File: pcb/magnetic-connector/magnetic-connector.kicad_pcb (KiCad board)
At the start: 2 copper layers, 26 x 24 mm, 14 parts, among them J10 MAG_CONN_IN, J7 VIK_IN, J8 VIK_OUT, J9 MAG_CONN_OUT

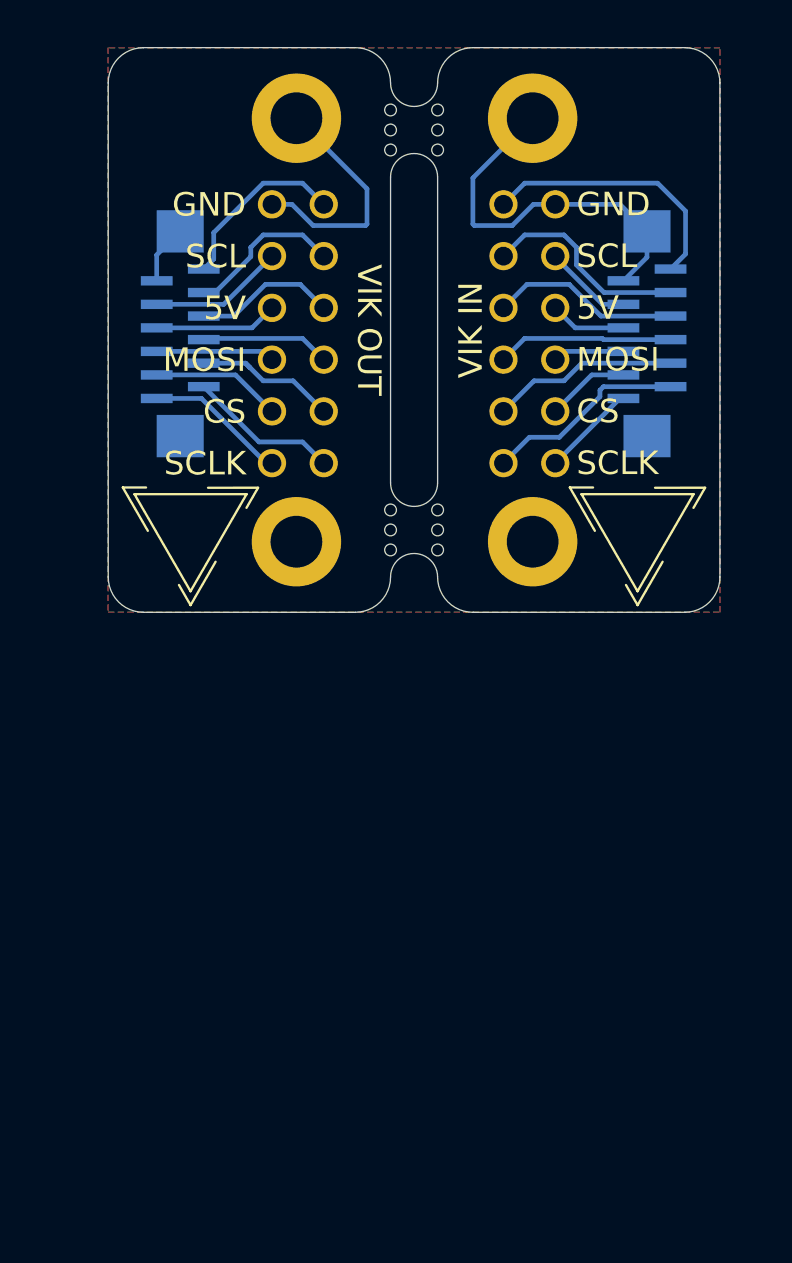
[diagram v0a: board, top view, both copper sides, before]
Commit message: Make magnetic connector size compliant with VIK small form factor.
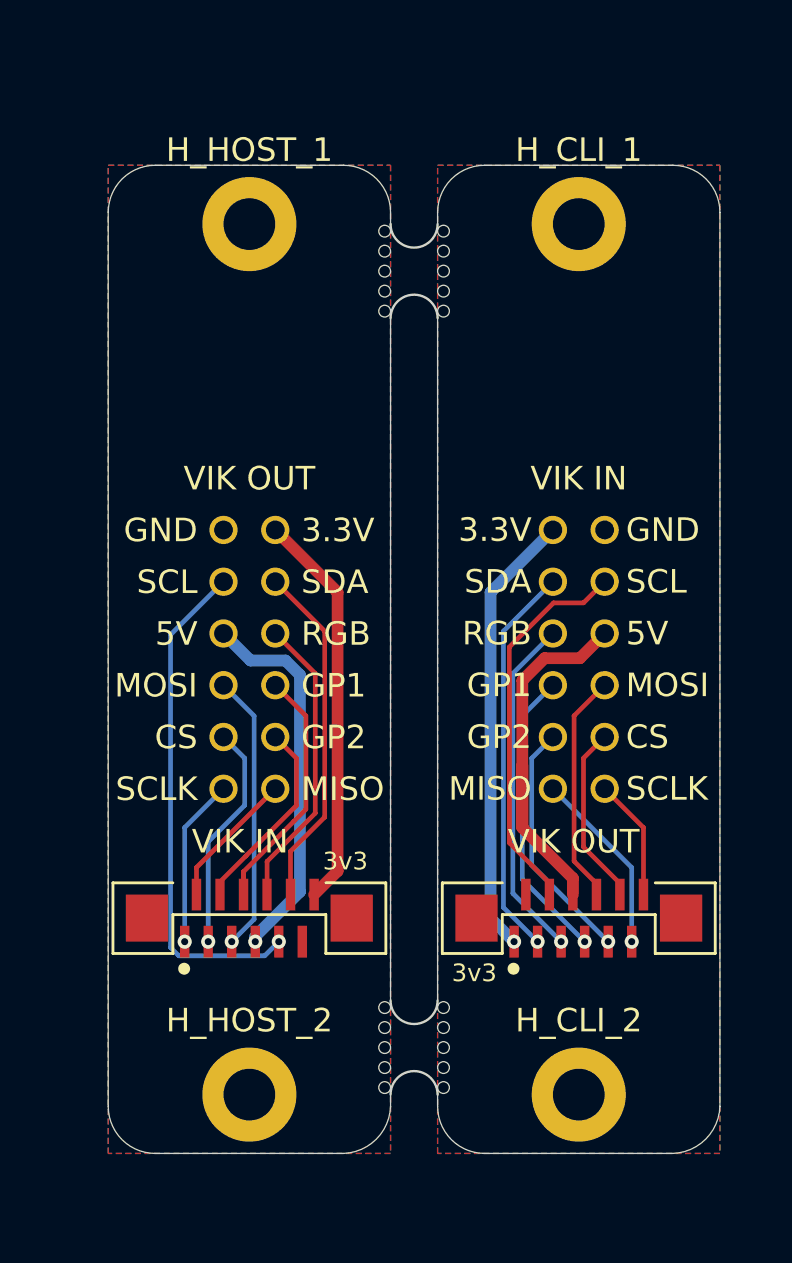
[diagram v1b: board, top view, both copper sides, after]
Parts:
- removed ? (x4): , 
- removed ? (x2): vik-logo-small, vik:vik-logo-small
- removed J10: MAG_CONN_IN, vik:vik-module-throughole-2.2mm
- removed J7: VIK_IN, vik:vik-module-connector-vertical
- removed J8: VIK_OUT, vik:vik-keyboard-connector-vertical
- removed J9: MAG_CONN_OUT, vik:vik-keyboard-throughole-2.2mm
- removed the REF** at (34.0, 35.5)
- removed the REF** at (34.0, 18.5)
- removed the REF** at (32.0, 35.5)
- removed the REF** at (32.0, 18.5)
- added H_CLI_1: MountingHole_Pad, MountingHole:MountingHole_2.2mm_M2_Pad, F.Cu at (40.0, 22.5)
- added H_CLI_2: MountingHole_Pad, MountingHole:MountingHole_2.2mm_M2_Pad, F.Cu at (40.0, 59.5)
- added H_HOST_1: MountingHole_Pad, MountingHole:MountingHole_2.2mm_M2_Pad, F.Cu at (26.0, 22.5)
- added H_HOST_2: MountingHole_Pad, MountingHole:MountingHole_2.2mm_M2_Pad, F.Cu at (26.0, 59.5)
- added J_MC_CLI1: MAG_CONN_IN, magnetic-connector:vik-module-throughole-2.2mm, F.Cu at (40.0, 39.9)
- added J_MC_HOST1: MAG_CONN_OUT, magnetic-connector:vik-keyboard-throughole-2.2mm, F.Cu at (26.0, 39.9)
- added J_VIK_CLI1: VIK_OUT, vik:vik-keyboard-connector-vertical, F.Cu at (40.0, 52.0)
- added J_VIK_HOST1: VIK_IN, vik:vik-module-connector-vertical, F.Cu at (26.0, 52.0)
- added REF**: MouseBite-Slot_2.0x2.0mm_inset_D0.5mm_P0.85mm_5h, Panelization:MouseBite-Slot_2.0x2.0mm_inset_D0.5mm_P0.85mm_5h, F.Cu at (34.0, 57.5)
- added REF**: MouseBite-Slot_2.0x2.0mm_inset_D0.5mm_P0.85mm_5h, Panelization:MouseBite-Slot_2.0x2.0mm_inset_D0.5mm_P0.85mm_5h, F.Cu at (34.0, 24.5)
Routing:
- net /gnd: track 29.0 -> 0.00 mm
- net Net-(J_MC_HOST1-SCL): track 0.00 -> 21.5 mm, vias 0 -> 1
- net Net-(J_MC_CLI1-3V3): track 0.00 -> 19.0 mm, vias 0 -> 1
- net Net-(J_MC_HOST1-3V3): track 0.00 -> 17.0 mm
- net Net-(J_MC_CLI1-5V): track 0.00 -> 17.0 mm
- net Net-(J_MC_CLI1-SDA): track 0.00 -> 16.8 mm, vias 0 -> 1
- net Net-(J_MC_CLI1-SCL): track 0.00 -> 16.4 mm
- net Net-(J_MC_HOST1-5V): track 0.00 -> 16.1 mm, vias 0 -> 1
- net Net-(J_MC_HOST1-SDA): track 0.00 -> 14.8 mm
- net Net-(J_MC_CLI1-RGB_DO): track 0.00 -> 14.7 mm, vias 0 -> 1
- net Net-(J_MC_HOST1-RGB_DO): track 0.00 -> 12.7 mm
- net Net-(J_MC_CLI1-GP_AD1): track 0.00 -> 12.5 mm, vias 0 -> 1
- net Net-(J_MC_HOST1-MOSI): track 0.00 -> 11.8 mm, vias 0 -> 1
- net Net-(J10-3V3): track 11.3 -> 0.00 mm
- net Net-(J_MC_HOST1-GP_AD1): track 0.00 -> 11.0 mm
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- added copper zone on B.Cu, net /GND_CLI
- added copper zone on F.Cu, net /GND_CLI
- added copper zone on B.Cu, net /GND_HOST
- added copper zone on F.Cu, net /GND_HOST
- removed copper zone on B.Cu, net /gnd
- removed copper zone on F.Cu, net /gnd
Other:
- board size 26 x 24 mm -> 26 x 42 mm

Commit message: Add ESD protection to magnetic connector module.
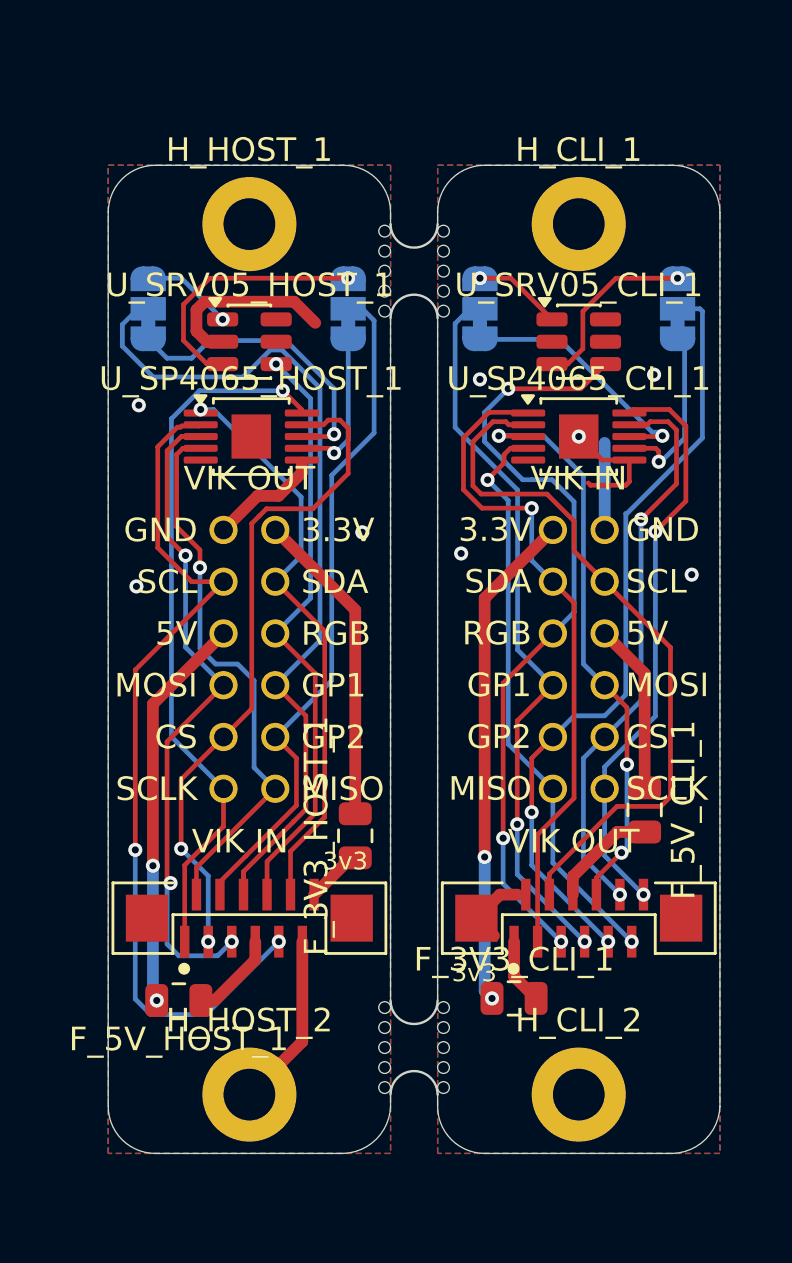
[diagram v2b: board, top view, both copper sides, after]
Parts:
- added F_3V3_CLI_1: SMD0805-050-16V, Fuse:Fuse_0805_2012Metric, F.Cu at (37.2, 55.4)
- added F_3V3_HOST_1: SMD0805-050-16V, Fuse:Fuse_0805_2012Metric, F.Cu at (30.5, 48.5)
- added F_5V_CLI_1: SMD0805-050-16V, Fuse:Fuse_0805_2012Metric, F.Cu at (42.8, 47.4)
- added F_5V_HOST_1: SMD0805-050-16V, Fuse:Fuse_0805_2012Metric, F.Cu at (23.0, 55.5)
- added JP1: SolderJumper_3_Bridged12, Jumper:SolderJumper-3_P1.3mm_Bridged12_RoundedPad1.0x1.5mm_NumberLabels, B.Cu at (21.7, 26.1)
- added JP2: SolderJumper_3_Bridged12, Jumper:SolderJumper-3_P1.3mm_Bridged12_RoundedPad1.0x1.5mm_NumberLabels, B.Cu at (30.2, 26.1)
- added JP3: SolderJumper_3_Bridged12, Jumper:SolderJumper-3_P1.3mm_Bridged12_RoundedPad1.0x1.5mm_NumberLabels, B.Cu at (35.8, 26.1)
- added JP4: SolderJumper_3_Bridged12, Jumper:SolderJumper-3_P1.3mm_Bridged12_RoundedPad1.0x1.5mm_NumberLabels, B.Cu at (44.2, 26.1)
- added U_SP4065_CLI_1: SP4065, Package_SO:MSOP-10-1EP_3x3mm_P0.5mm_EP1.68x1.88mm, F.Cu at (40.0, 31.5)
- added U_SP4065_HOST_1: SP4065, Package_SO:MSOP-10-1EP_3x3mm_P0.5mm_EP1.68x1.88mm, F.Cu at (26.1, 31.5)
- added U_SRV05_CLI_1: SRV05-4, Package_TO_SOT_SMD:SOT-23-6, F.Cu at (40.0, 27.5)
- added U_SRV05_HOST_1: SRV05-4, Package_TO_SOT_SMD:SOT-23-6, F.Cu at (26.0, 27.5)
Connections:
- net /GND_CLI renamed /Client/GND
- net /GND_HOST renamed /Host/GND
- net Net-(J_MC_CLI1-GP_AD1) renamed /Client/GP1_D+
- net Net-(J_MC_CLI1-GP_AD2) renamed /Client/GP2_D-
- net Net-(J_MC_CLI1-MISO) renamed /Client/MISO
- net Net-(J_MC_CLI1-MOSI) renamed /Client/MOSI
- net Net-(J_MC_CLI1-RGB_DO) renamed /Client/RGB_DO
- net Net-(J_MC_CLI1-SCL) renamed /Client/SCL
- net Net-(J_MC_CLI1-SCLK) renamed /Client/SCLK
- net Net-(J_MC_CLI1-SDA) renamed /Client/SDA
- net Net-(J_MC_CLI1-SPI_CS) renamed /Client/CS
- net Net-(J_MC_HOST1-GP_AD1) renamed /Host/GP1_D+
- net Net-(J_MC_HOST1-GP_AD2) renamed /Host/GP2_D-
- net Net-(J_MC_HOST1-MISO) renamed /Host/MISO
- net Net-(J_MC_HOST1-MOSI) renamed /Host/MOSI
- net Net-(J_MC_HOST1-RGB_DO) renamed /Host/RGB_DO
- net Net-(J_MC_HOST1-SCL) renamed /Host/SCL
- net Net-(J_MC_HOST1-SCLK) renamed /Host/SCLK
- net Net-(J_MC_HOST1-SDA) renamed /Host/SDA
- net Net-(J_MC_HOST1-SPI_CS) renamed /Host/CS
- J_MC_CLI1 pad 12: Net-(J_MC_CLI1-3V3) -> /Client/3V3_IN
- J_MC_CLI1 pad 7: Net-(J_MC_CLI1-5V) -> /Client/5V_IN
- J_MC_HOST1 pad 1: Net-(J_MC_HOST1-3V3) -> /Host/3V3_OUT
- J_MC_HOST1 pad 6: Net-(J_MC_HOST1-5V) -> /Host/5V_OUT
- J_VIK_CLI1 pad 1: Net-(J_MC_CLI1-3V3) -> /Client/3V3_OUT
- J_VIK_CLI1 pad 6: Net-(J_MC_CLI1-5V) -> /Client/5V_OUT
- J_VIK_HOST1 pad 12: Net-(J_MC_HOST1-3V3) -> /Host/3V3_IN
- J_VIK_HOST1 pad 7: Net-(J_MC_HOST1-5V) -> /Host/5V_IN
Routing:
- net /Host/GP1_D+: track 11.0 -> 36.8 mm
- net /Host/SCLK: track 7.18 -> 30.3 mm
- net /Client/GP2_D-: track 10.4 -> 33.0 mm, vias 1 -> 2
- net /Client/3V3_IN: track 0.00 -> 21.2 mm, vias 0 -> 2
- net /Host/GP2_D-: track 8.42 -> 29.2 mm
- net /Host/GND: track 0.00 -> 20.0 mm, vias 0 -> 3
- net /Client/SCLK: track 5.18 -> 24.8 mm, vias 0 -> 2
- net Net-(J_MC_CLI1-3V3): track 19.0 -> 0.00 mm, vias 1 -> 0
- net /Host/CS: track 9.71 -> 28.6 mm, vias 1 -> 2
- net /Client/GP1_D+: track 12.5 -> 31.1 mm, vias 1 -> 2
- net /Client/RGB_DO: track 14.7 -> 33.1 mm, vias 1 -> 3
- net /Host/MISO: track 5.39 -> 23.0 mm, vias 0 -> 1
- net Net-(J_MC_HOST1-3V3): track 17.0 -> 0.00 mm
- net Net-(J_MC_CLI1-5V): track 17.0 -> 0.00 mm
- net /Host/5V_OUT: track 0.00 -> 16.9 mm, vias 0 -> 2
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
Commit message: Change VIK connector and ESD protection chips.
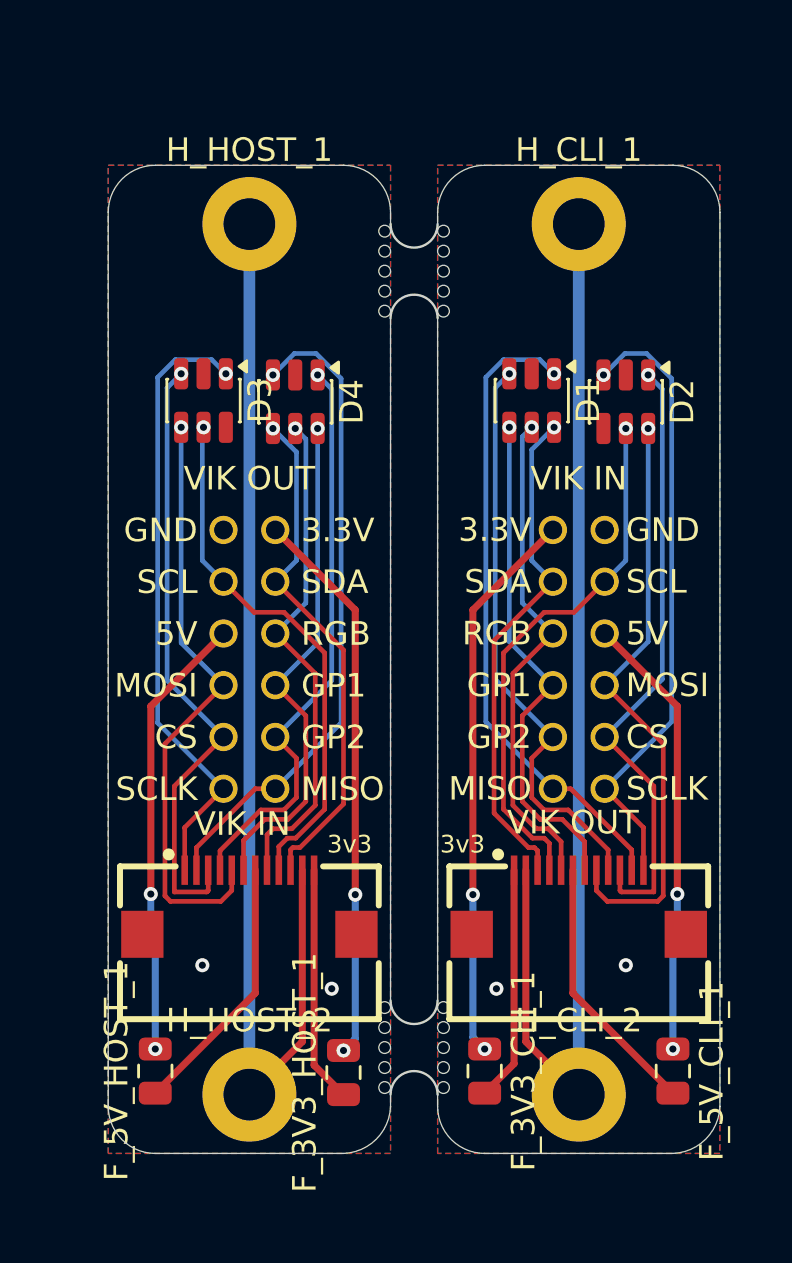
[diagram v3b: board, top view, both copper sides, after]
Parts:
- removed JP1, JP2, JP3, JP4: SolderJumper_3_Bridged12, Jumper:SolderJumper-3_P1.3mm_Bridged12_RoundedPad1.0x1.5mm_NumberLabels
- removed U_SP4065_CLI_1, U_SP4065_HOST_1: SP4065, Package_SO:MSOP-10-1EP_3x3mm_P0.5mm_EP1.68x1.88mm
- removed U_SRV05_CLI_1, U_SRV05_HOST_1: SRV05-4, Package_TO_SOT_SMD:SOT-23-6
- added D1: ESDA6V1-5SC6, Package_TO_SOT_SMD:SOT-23-6, F.Cu at (38.0, 30.0)
- added D2: ESDA6V1-5SC6, Package_TO_SOT_SMD:SOT-23-6, F.Cu at (42.0, 30.1)
- added D3: ESDA6V1-5SC6, Package_TO_SOT_SMD:SOT-23-6, F.Cu at (24.1, 30.0)
- added D4: ESDA6V1-5SC6, Package_TO_SOT_SMD:SOT-23-6, F.Cu at (27.9, 30.1)
- J_VIK_CLI1: footprint vik:vik-keyboard-connector-vertical -> vik:vik-keyboard-connector-horizontal
- J_VIK_HOST1: footprint vik:vik-module-connector-vertical -> vik:vik-module-connector-horizontal
- moved F_5V_CLI_1 11.2 mm to (44.0, 58.5)
- moved F_3V3_HOST_1 10.1 mm to (30.0, 58.6)
- moved F_3V3_CLI_1 3.33 mm to (36.0, 58.5), turned to -90 degrees
- moved F_5V_HOST_1 3.16 mm to (22.0, 58.5), turned to 90 degrees
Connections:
- J_MC_CLI1 pad 4: /Client/GP2_D- -> /Client/GP2
- J_MC_CLI1 pad 6: /Client/GP1_D+ -> /Client/GP1
- J_MC_HOST1 pad 7: /Host/GP1_D+ -> /Host/GP1
- J_MC_HOST1 pad 9: /Host/GP2_D- -> /Host/GP2
- J_VIK_CLI1 pad 7: /Client/GP1_D+ -> /Client/GP1
- J_VIK_CLI1 pad 9: /Client/GP2_D- -> /Client/GP2
- J_VIK_HOST1 pad 4: /Host/GP2_D- -> /Host/GP2
- J_VIK_HOST1 pad 6: /Host/GP1_D+ -> /Host/GP1
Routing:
- net /Host/GP1_D+: track 36.8 -> 0.00 mm
- net /Client/GND: track 12.3 -> 47.5 mm, vias 5 -> 2
- net /Client/GP2_D-: track 33.0 -> 0.00 mm, vias 2 -> 0
- net /Client/GP1_D+: track 31.1 -> 0.00 mm, vias 2 -> 0
- net /Host/GP2_D-: track 29.2 -> 0.00 mm
- net /Host/GND: track 20.0 -> 47.5 mm, vias 3 -> 2
- net /Host/GP2: track 6.56 -> 24.6 mm
- net /Client/GP2: track 7.58 -> 24.7 mm
- net /Host/SCL: track 36.8 -> 22.8 mm, vias 2 -> 1
- net /Client/5V_IN: track 7.27 -> 19.0 mm, vias 0 -> 2
- net /Client/RGB_DO: track 33.1 -> 21.4 mm, vias 3 -> 1
- net /Host/D-: track 11.1 -> 0.00 mm, vias 1 -> 0
- net /Client/GP1: track 10.9 -> 21.8 mm
- net /Host/3V3_OUT: track 13.5 -> 23.7 mm, vias 0 -> 2
- net /Host/GP1: track 12.7 -> 21.7 mm
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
